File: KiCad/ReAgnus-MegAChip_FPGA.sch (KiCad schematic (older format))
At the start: 7 parts, among them J1 Conn_02x02_Odd_Even, J2 Conn_02x05_Odd_Even, U10 AS4C4M16SA, U7 GW1N-UV9LQ144, X1 SG-8002CA

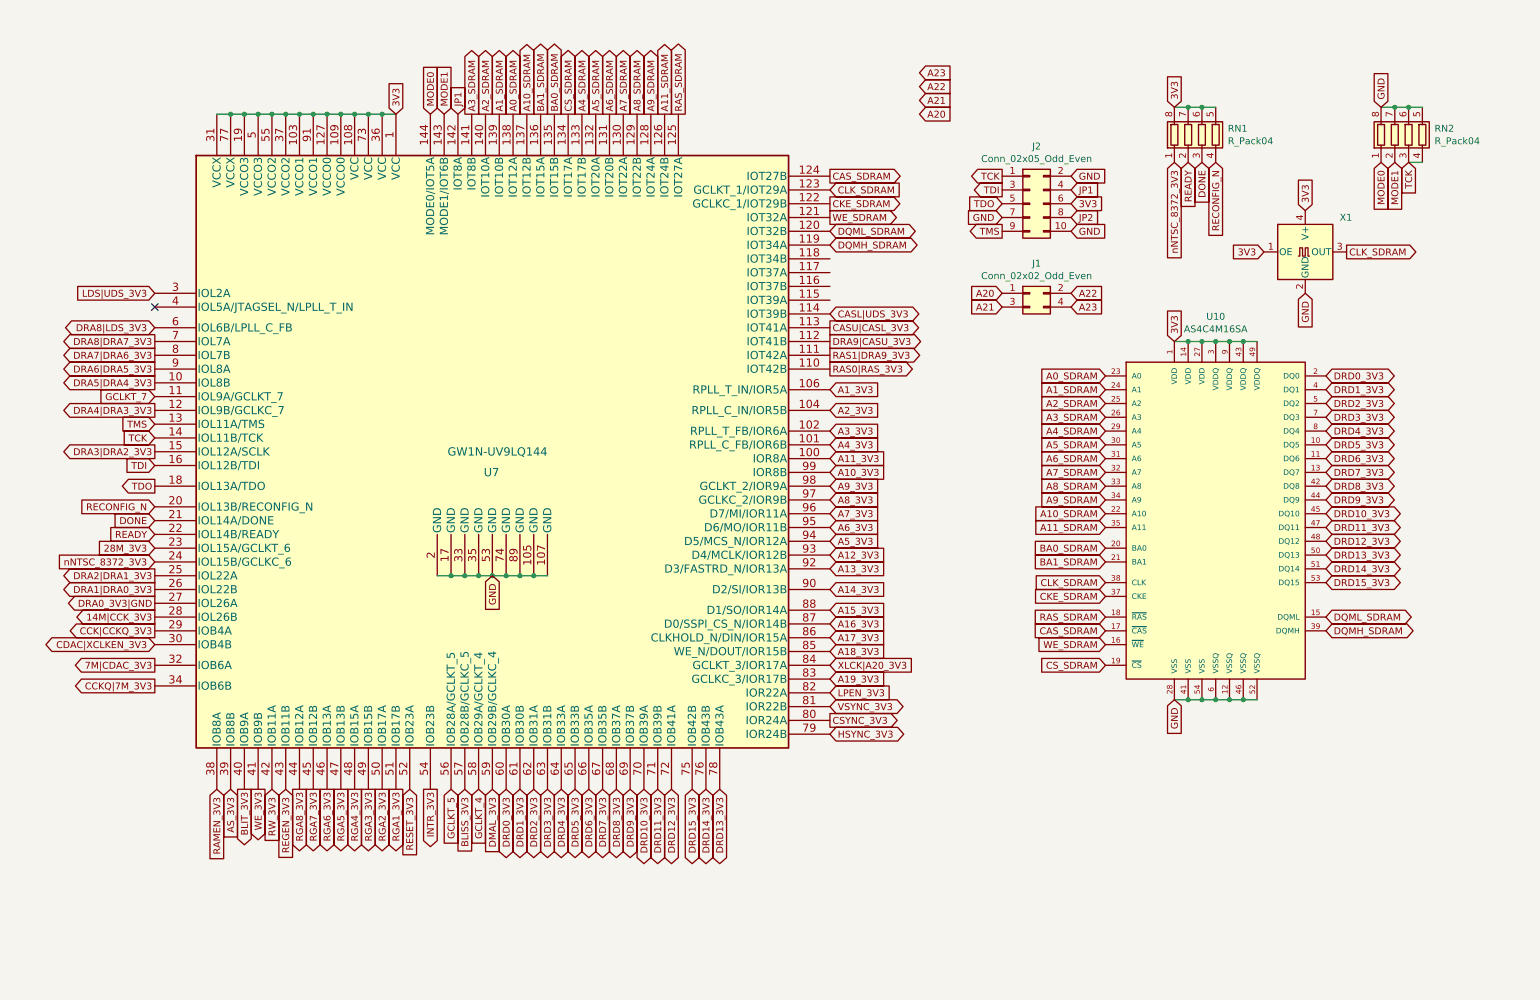
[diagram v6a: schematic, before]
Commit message: added 74LVC245A IC for A20-A23 and more routing done
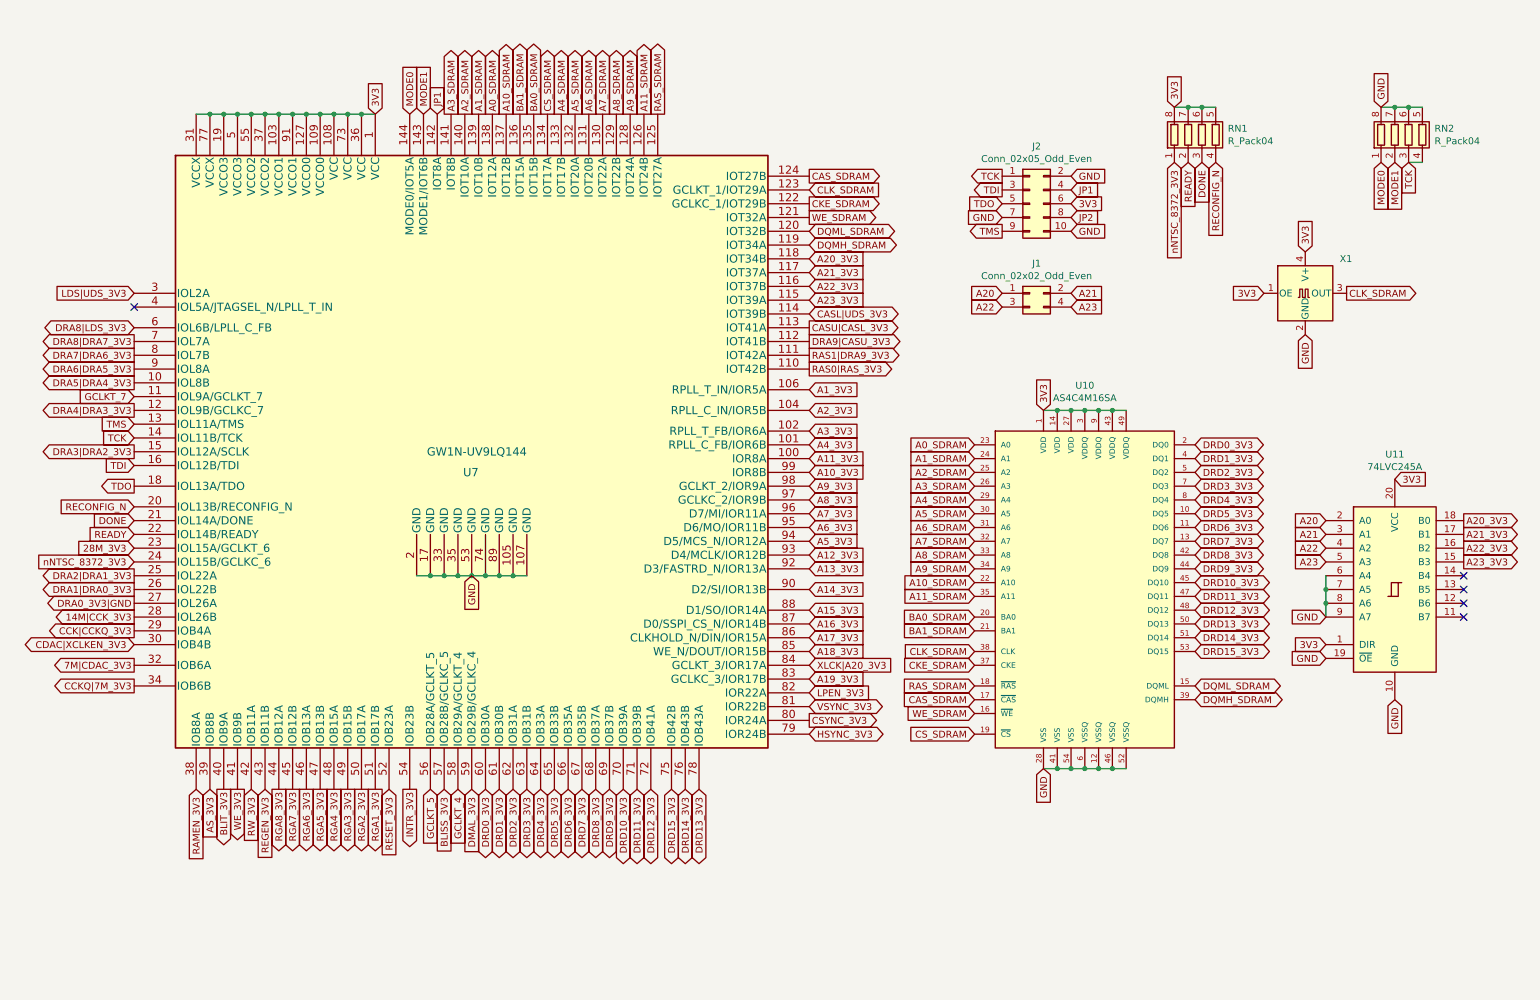
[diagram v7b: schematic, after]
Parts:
- added U11: 74LVC245A, Package_SO:TSSOP-20_4.4x6.5mm_P0.65mm, symbol ReAgnus-MegAChip:74LVC245A
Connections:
- net 3V3: now also U11.1 (DIR), U11.20 (VCC)
- net A20: now also U11.2 (A0)
- net A21: now also J1.2 (Pin_2), U11.3 (A1); no longer J1.3 (Pin_3)
- net A22: now also J1.3 (Pin_3), U11.4 (A2); no longer J1.2 (Pin_2)
- net A23: now also U11.5 (A3)
- net GND: now also U11.10 (GND), U11.19 (~OE), U11.6 (A4), U11.7 (A5), U11.8 (A6), U11.9 (A7)
- net A23_3V3: now reaches U7.115 (IOT39A)
- net A23_3V3: now also U11.15 (B3)
- net A22_3V3: now reaches U7.116 (IOT37B)
- net A22_3V3: now also U11.16 (B2)
- net A21_3V3: now reaches U7.117 (IOT37A)
- net A21_3V3: now also U11.17 (B1)
- net A20_3V3: now reaches U7.118 (IOT34B)
- net A20_3V3: now also U11.18 (B0)
- no-connect marks 1 -> 5
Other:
- moved on the sheet: U10, U7, X1

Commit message: more routing and placing components
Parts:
- added U12: 74LVC1GX04, Package_SO:TSOP-6_1.65x3.05mm_P0.95mm, symbol ReAgnus-MegAChip:74LVC1GX04
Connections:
- net GCLKT_5 is gone; now on net JP2: U7.56 (IOB28A/GCLKT_5)
- net 3V3: now also U12.5 (VCC)
- net GCLKT_7: now also U12.6 (Y)
- net GND: now also U12.2 (GND)
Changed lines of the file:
@@
 Text GLabel 1300 3100 0    50   Input ~ 0
 GCLKT_7
-Text GLabel 3450 5950 3    50   Input ~ 0
-GCLKT_5
 Text GLabel 3650 5950 3    50   Input ~ 0
 GCLKT_4
@@
 NoConn ~ 10950 4600
 NoConn ~ 10950 4700
+$Comp
+L ReAgnus-MegAChip:74LVC1GX04 U12
+U 1 1 637F9038
+P 5900 7050
+F 0 "U12" H 5900 7565 50  0000 C CNN
+F 1 "74LVC1GX04" H 5900 7474 50  0000 C CNN
+F 2 "Package_SO:TSOP-6_1.65x3.05mm_P0.95mm" H 6400 8000 50  0001 C CNN
+F 3 "https://www.mouser.se/datasheet/2/916/74LVC1GX04-2937637.pdf" H 6400 8000 50  0001 C CNN
+	1    5900 7050
+	1    0    0    -1
+$EndComp
+Text GLabel 5450 7050 0    50   Input ~ 0
+GND
+Text GLabel 6350 7050 2    50   Input ~ 0
+3V3
+Text GLabel 6350 6850 2    50   Input ~ 0
+GCLKT_7
+Text GLabel 3450 5950 3    50   Input ~ 0
+JP2
 $EndSCHEMATC
